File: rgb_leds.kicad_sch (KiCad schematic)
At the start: 11 parts

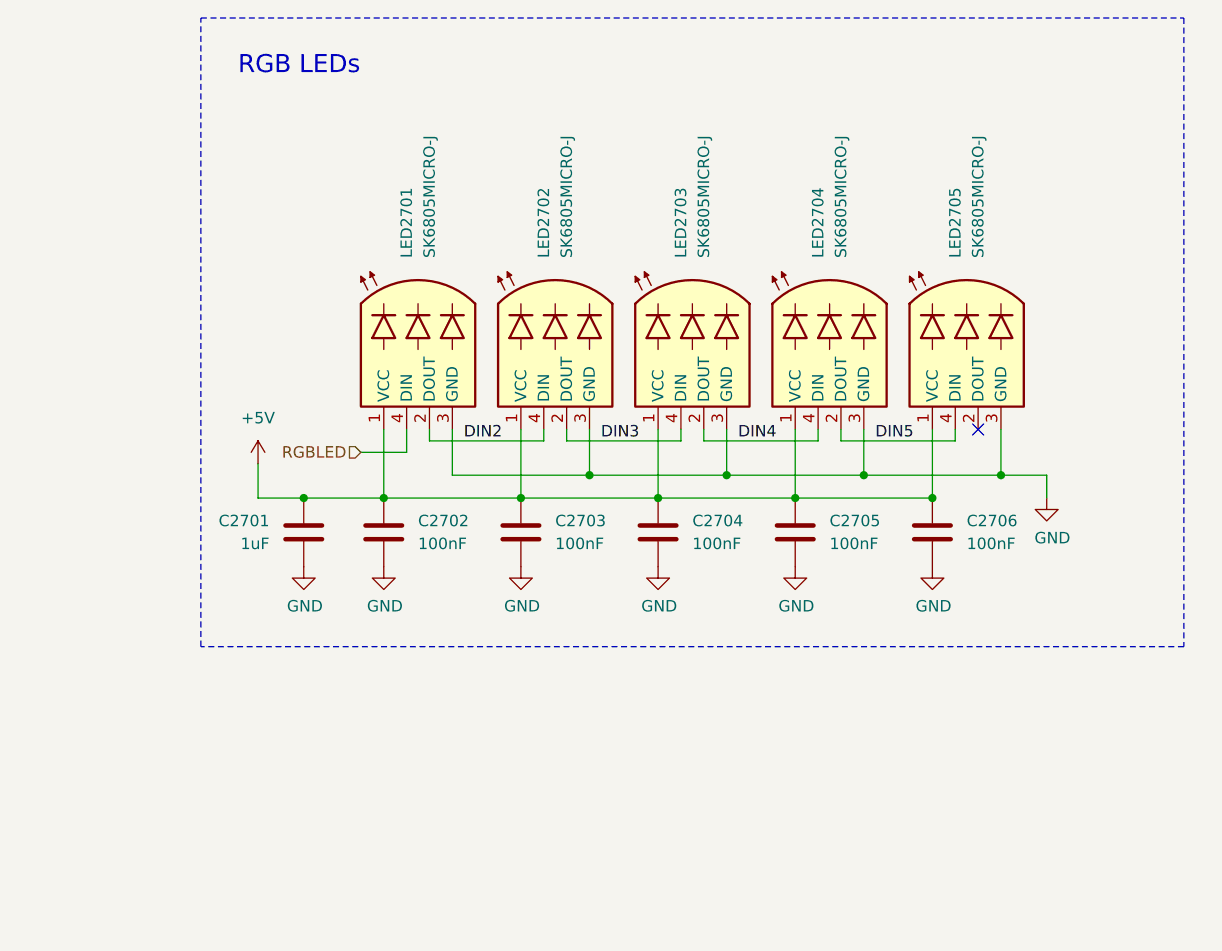
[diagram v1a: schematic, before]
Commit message: Reannotate components
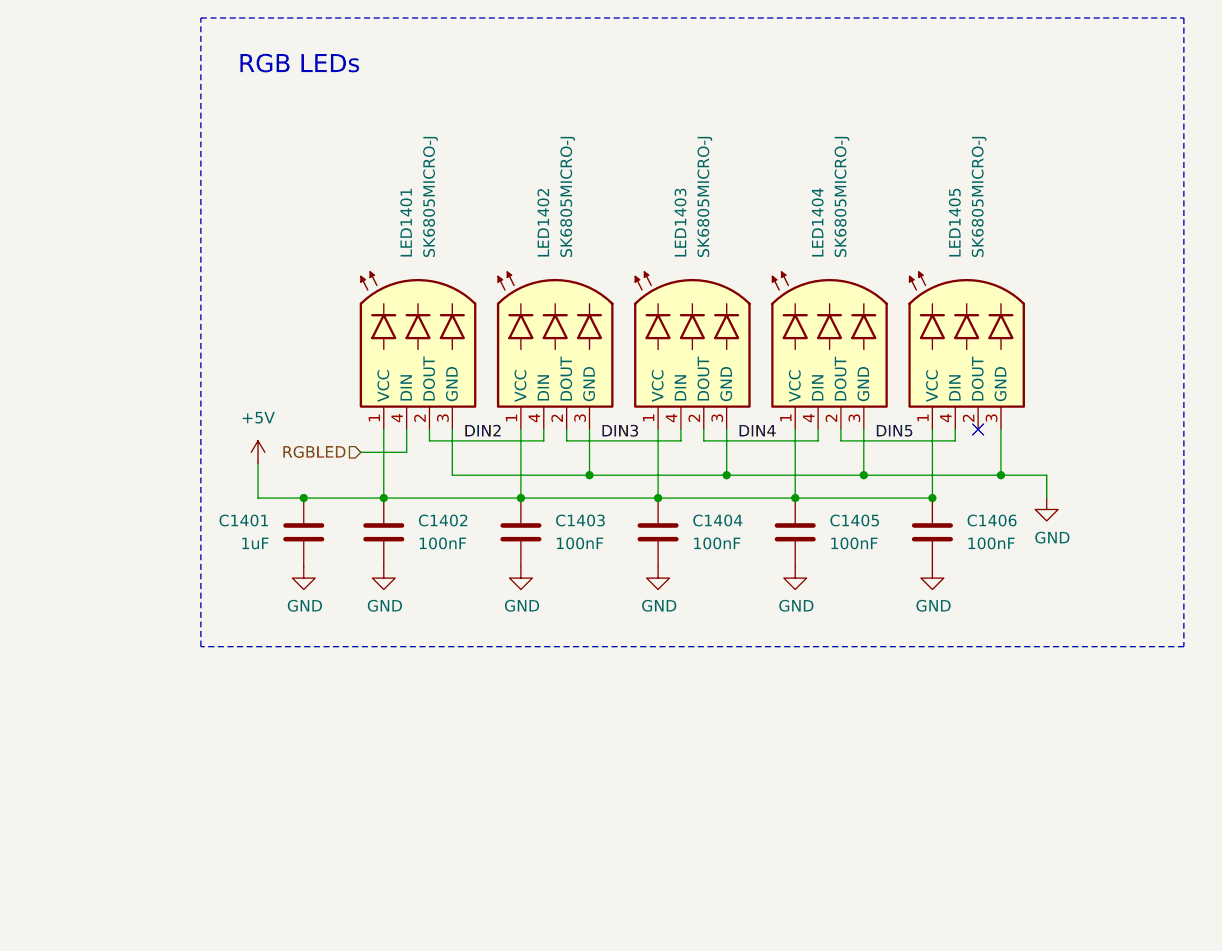
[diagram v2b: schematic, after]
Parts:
- renumbered C2701 to C1401, C2702 to C1402, C2703 to C1403, C2704 to C1404, C2705 to C1405, C2706 to C1406, LED2701 to LED1401, LED2702 to LED1402, LED2703 to LED1403, LED2704 to LED1404, LED2705 to LED1405
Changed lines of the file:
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@@
 		(dnp no)
 		(fields_autoplaced yes)
-		(property "Reference" "C2703"
+		(property "Reference" "C1403"
 			(at 125.73 119.3799 0)
 			(effects
@@
 			(project "HALPI2"
 				(path "/abc482bd-3f17-4d35-80db-1da3dcdb5c27/850df4bf-e40a-4082-adc2-76804638b949/7441bc5f-8874-43c2-af8a-50459ea25028"
-					(reference "C2703")
+					(reference "C1403")
 					(unit 1)
 				)
@@
 		(on_board yes)
 		(dnp no)
-		(property "Reference" "#PWR02703"
+		(property "Reference" "#PWR01402"
 			(at 97.79 130.81 0)
 			(effects
@@
 			(project "HALPI2"
 				(path "/abc482bd-3f17-4d35-80db-1da3dcdb5c27/850df4bf-e40a-4082-adc2-76804638b949/7441bc5f-8874-43c2-af8a-50459ea25028"
-					(reference "#PWR02703")
+					(reference "#PWR01402")
 					(unit 1)
 				)
@@
 		(dnp no)
 		(fields_autoplaced yes)
-		(property "Reference" "C2705"
+		(property "Reference" "C1405"
 			(at 156.21 119.3799 0)
 			(effects
@@
 			(project "HALPI2"
 				(path "/abc482bd-3f17-4d35-80db-1da3dcdb5c27/850df4bf-e40a-4082-adc2-76804638b949/7441bc5f-8874-43c2-af8a-50459ea25028"
-					(reference "C2705")
+					(reference "C1405")
 					(unit 1)
 				)
@@
 		(dnp no)
 		(fields_autoplaced yes)
-		(property "Reference" "C2704"
+		(property "Reference" "C1404"
 			(at 140.97 119.3799 0)
 			(effects
@@
 			(project "HALPI2"
 				(path "/abc482bd-3f17-4d35-80db-1da3dcdb5c27/850df4bf-e40a-4082-adc2-76804638b949/7441bc5f-8874-43c2-af8a-50459ea25028"
-					(reference "C2704")
+					(reference "C1404")
 					(unit 1)
 				)
@@
 		(on_board yes)
 		(dnp no)
-		(property "Reference" "#PWR02707"
+		(property "Reference" "#PWR01406"
 			(at 152.4 130.81 0)
 			(effects
@@
 			(project "HALPI2"
 				(path "/abc482bd-3f17-4d35-80db-1da3dcdb5c27/850df4bf-e40a-4082-adc2-76804638b949/7441bc5f-8874-43c2-af8a-50459ea25028"
-					(reference "#PWR02707")
+					(reference "#PWR01406")
 					(unit 1)
 				)
@@
 		(on_board yes)
 		(dnp no)
-		(property "Reference" "#PWR02704"
+		(property "Reference" "#PWR01403"
 			(at 106.68 130.81 0)
 			(effects
@@
 			(project "HALPI2"
 				(path "/abc482bd-3f17-4d35-80db-1da3dcdb5c27/850df4bf-e40a-4082-adc2-76804638b949/7441bc5f-8874-43c2-af8a-50459ea25028"
-					(reference "#PWR02704")
+					(reference "#PWR01403")
 					(unit 1)
 				)
@@
 		(dnp no)
 		(fields_autoplaced yes)
-		(property "Reference" "#PWR02701"
+		(property "Reference" "#PWR01401"
 			(at 92.71 116.84 0)
 			(effects
@@
 			(project "HALPI2"
 				(path "/abc482bd-3f17-4d35-80db-1da3dcdb5c27/850df4bf-e40a-4082-adc2-76804638b949/7441bc5f-8874-43c2-af8a-50459ea25028"
-					(reference "#PWR02701")
+					(reference "#PWR01401")
 					(unit 1)
 				)
@@
 		(on_board yes)
 		(dnp no)
-		(property "Reference" "#PWR02702"
+		(property "Reference" "#PWR01408"
 			(at 180.34 123.19 0)
 			(effects
@@
 			(project "HALPI2"
 				(path "/abc482bd-3f17-4d35-80db-1da3dcdb5c27/850df4bf-e40a-4082-adc2-76804638b949/7441bc5f-8874-43c2-af8a-50459ea25028"
-					(reference "#PWR02702")
+					(reference "#PWR01408")
 					(unit 1)
 				)
@@
 		(on_board yes)
 		(dnp no)
-		(property "Reference" "C2701"
+		(property "Reference" "C1401"
 			(at 93.98 119.3799 0)
 			(effects
@@
 			(project "HALPI2"
 				(path "/abc482bd-3f17-4d35-80db-1da3dcdb5c27/850df4bf-e40a-4082-adc2-76804638b949/7441bc5f-8874-43c2-af8a-50459ea25028"
-					(reference "C2701")
+					(reference "C1401")
 					(unit 1)
 				)
@@
 		(on_board yes)
 		(dnp no)
-		(property "Reference" "#PWR02708"
+		(property "Reference" "#PWR01407"
 			(at 167.64 130.81 0)
 			(effects
@@
 			(project "HALPI2"
 				(path "/abc482bd-3f17-4d35-80db-1da3dcdb5c27/850df4bf-e40a-4082-adc2-76804638b949/7441bc5f-8874-43c2-af8a-50459ea25028"
-					(reference "#PWR02708")
+					(reference "#PWR01407")
 					(unit 1)
 				)
@@
 		(dnp no)
 		(fields_autoplaced yes)
-		(property "Reference" "LED2702"
+		(property "Reference" "LED1402"
 			(at 124.4599 90.17 0)
 			(effects
@@
 			(project "HALPI2"
 				(path "/abc482bd-3f17-4d35-80db-1da3dcdb5c27/850df4bf-e40a-4082-adc2-76804638b949/7441bc5f-8874-43c2-af8a-50459ea25028"
-					(reference "LED2702")
+					(reference "LED1402")
 					(unit 1)
 				)
@@
 		(on_board yes)
 		(dnp no)
-		(property "Reference" "#PWR02706"
+		(property "Reference" "#PWR01405"
 			(at 137.16 130.81 0)
 			(effects
@@
 			(project "HALPI2"
 				(path "/abc482bd-3f17-4d35-80db-1da3dcdb5c27/850df4bf-e40a-4082-adc2-76804638b949/7441bc5f-8874-43c2-af8a-50459ea25028"
-					(reference "#PWR02706")
+					(reference "#PWR01405")
 					(unit 1)
 				)
@@
 		(dnp no)
 		(fields_autoplaced yes)
-		(property "Reference" "LED2704"
+		(property "Reference" "LED1404"
 			(at 154.9399 90.17 0)
 			(effects
@@
 			(project "HALPI2"
 				(path "/abc482bd-3f17-4d35-80db-1da3dcdb5c27/850df4bf-e40a-4082-adc2-76804638b949/7441bc5f-8874-43c2-af8a-50459ea25028"
-					(reference "LED2704")
+					(reference "LED1404")
 					(unit 1)
 				)
@@
 		(dnp no)
 		(fields_autoplaced yes)
-		(property "Reference" "C2706"
+		(property "Reference" "C1406"
 			(at 171.45 119.3799 0)
 			(effects
@@
 			(project "HALPI2"
 				(path "/abc482bd-3f17-4d35-80db-1da3dcdb5c27/850df4bf-e40a-4082-adc2-76804638b949/7441bc5f-8874-43c2-af8a-50459ea25028"
-					(reference "C2706")
+					(reference "C1406")
 					(unit 1)
 				)
@@
 		(dnp no)
 		(fields_autoplaced yes)
-		(property "Reference" "C2702"
+		(property "Reference" "C1402"
 			(at 110.49 119.3799 0)
 			(effects
@@
 			(project "HALPI2"
 				(path "/abc482bd-3f17-4d35-80db-1da3dcdb5c27/850df4bf-e40a-4082-adc2-76804638b949/7441bc5f-8874-43c2-af8a-50459ea25028"
-					(reference "C2702")
+					(reference "C1402")
 					(unit 1)
 				)
@@
 		(dnp no)
 		(fields_autoplaced yes)
-		(property "Reference" "LED2703"
+		(property "Reference" "LED1403"
 			(at 139.6999 90.17 0)
 			(effects
@@
 			(project "HALPI2"
 				(path "/abc482bd-3f17-4d35-80db-1da3dcdb5c27/850df4bf-e40a-4082-adc2-76804638b949/7441bc5f-8874-43c2-af8a-50459ea25028"
-					(reference "LED2703")
+					(reference "LED1403")
 					(unit 1)
 				)
@@
 		(dnp no)
 		(fields_autoplaced yes)
-		(property "Reference" "LED2705"
+		(property "Reference" "LED1405"
 			(at 170.1799 90.17 0)
 			(effects
@@
 			(project "HALPI2"
 				(path "/abc482bd-3f17-4d35-80db-1da3dcdb5c27/850df4bf-e40a-4082-adc2-76804638b949/7441bc5f-8874-43c2-af8a-50459ea25028"
-					(reference "LED2705")
+					(reference "LED1405")
 					(unit 1)
 				)
@@
 		(dnp no)
 		(fields_autoplaced yes)
-		(property "Reference" "LED2701"
+		(property "Reference" "LED1401"
 			(at 109.2199 90.17 0)
 			(effects
@@
 			(project "HALPI2"
 				(path "/abc482bd-3f17-4d35-80db-1da3dcdb5c27/850df4bf-e40a-4082-adc2-76804638b949/7441bc5f-8874-43c2-af8a-50459ea25028"
-					(reference "LED2701")
+					(reference "LED1401")
 					(unit 1)
 				)
@@
 		(on_board yes)
 		(dnp no)
-		(property "Reference" "#PWR02705"
+		(property "Reference" "#PWR01404"
 			(at 121.92 130.81 0)
 			(effects
@@
 			(project "HALPI2"
 				(path "/abc482bd-3f17-4d35-80db-1da3dcdb5c27/850df4bf-e40a-4082-adc2-76804638b949/7441bc5f-8874-43c2-af8a-50459ea25028"
-					(reference "#PWR02705")
-					(unit 1)
-				)
+					(reference "#PWR01404")
+					(unit 1)
+				)

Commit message: Silkscreen mostly done
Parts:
- C1401: value 1uF -> 10uF; footprint Capacitor_SMD:C_0402_1005Metric -> Capacitor_SMD:C_0603_1608Metric; LCSC C52923 -> C19702
- C1402, C1403, C1404, C1405, C1406: value 100nF -> 1uF; LCSC C1525 -> C52923
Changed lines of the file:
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@@
 			)
 		)
-		(property "Value" "100nF"
+		(property "Value" "1uF"
 			(at 125.73 121.9199 0)
 			(effects
@@
 			)
 		)
-		(property "LCSC" "C1525"
+		(property "LCSC" "C52923"
 			(at 121.92 120.65 0)
 			(effects
@@
 			)
 		)
-		(property "Value" "100nF"
+		(property "Value" "1uF"
 			(at 156.21 121.9199 0)
 			(effects
@@
 			)
 		)
-		(property "LCSC" "C1525"
+		(property "LCSC" "C52923"
 			(at 152.4 120.65 0)
 			(effects
@@
 			)
 		)
-		(property "Value" "100nF"
+		(property "Value" "1uF"
 			(at 140.97 121.9199 0)
 			(effects
@@
 			)
 		)
-		(property "LCSC" "C1525"
+		(property "LCSC" "C52923"
 			(at 137.16 120.65 0)
 			(effects
@@
 			)
 		)
-		(property "Value" "1uF"
+		(property "Value" "10uF"
 			(at 93.98 121.9199 0)
 			(effects
@@
 			)
 		)
-		(property "Footprint" "Capacitor_SMD:C_0402_1005Metric"
+		(property "Footprint" "Capacitor_SMD:C_0603_1608Metric"
 			(at 96.8248 124.46 0)
 			(effects
@@
 			)
 		)
-		(property "LCSC" "C52923"
+		(property "LCSC" "C19702"
 			(at 97.79 120.65 0)
 			(effects
@@
 			)
 		)
-		(property "Value" "100nF"
+		(property "Value" "1uF"
 			(at 171.45 121.9199 0)
 			(effects
@@
 			)
 		)
-		(property "LCSC" "C1525"
+		(property "LCSC" "C52923"
 			(at 167.64 120.65 0)
 			(effects
@@
 			)
 		)
-		(property "Value" "100nF"
+		(property "Value" "1uF"
 			(at 110.49 121.9199 0)
 			(effects
@@
 			)
 		)
-		(property "LCSC" "C1525"
+		(property "LCSC" "C52923"
 			(at 106.68 120.65 0)
 			(effects
